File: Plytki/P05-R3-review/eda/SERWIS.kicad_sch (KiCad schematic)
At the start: 22 parts

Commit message: P05 R3 (S1) etap 2: typy części — SMD 1206, posiadane THT z rejestru, SW1 JS202011AQN
Rezystory precyzyjne 1206 0,1 %: okno DAQ_OK (R3-R8) 10 ppm/K, dzielniki
kanałów 25 ppm/K. Z rejestru: 47k i 4,7k MF0207 na stojąco, MKT 10n/100n,
MKS2 1u, C0G 1n, logika i 1N4148. Wyjątki: R1 1 W leżący, C1, C12/C13 1210.
SW1: suwak kątowy C&K JS202011AQN (biegun B lustrzany względem 7201).
ERC 0, 464/464 pinów.

Co-Authored-By: Claude Opus 5.5 <noreply@anthropic.com>
Claude-Session: https://claude.ai/code/session_01PNjhiJP63vXoN5NGrWe8up
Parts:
- R36, R37, R38, R44, R45, R46, R47, R48, R49, R50, R51, R52, R55: footprint Resistor_SMD:R_0805_2012Metric -> Resistor_SMD:R_1206_3216Metric_Pad1.30x1.75mm_HandSolder; MPN 0805 1% 0.125W 1K -> RC1206FR-071KL
- R39, R40, R41, R42, R53, R54: footprint Resistor_SMD:R_0805_2012Metric -> Resistor_SMD:R_1206_3216Metric_Pad1.30x1.75mm_HandSolder; MPN 0805 1% 0.125W 10K -> RC1206FR-0710KL
- R43: footprint Resistor_SMD:R_0805_2012Metric -> Resistor_THT:R_Axial_DIN0207_L6.3mm_D2.5mm_P5.08mm_Vertical; MPN 0805 1% 0.125W 4.7K -> MF0207FTE-4K7 (Yageo MF0207 1% 0.6W, owned, standing)

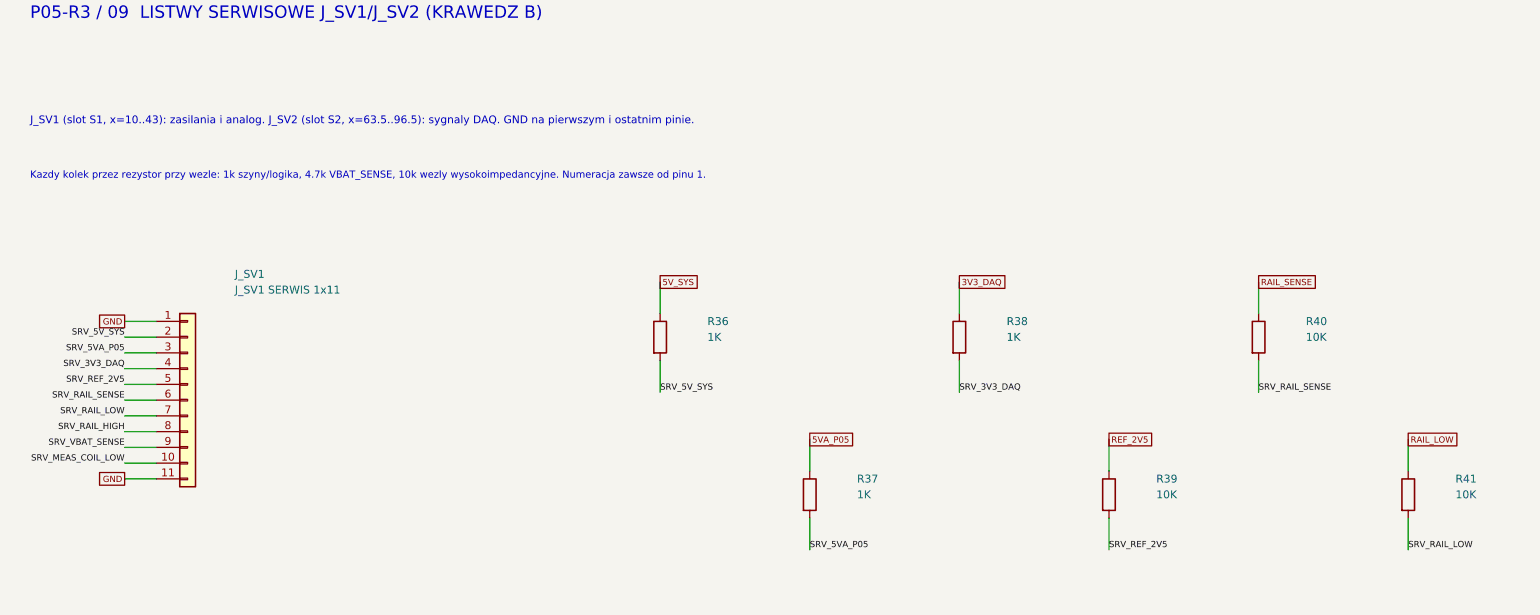
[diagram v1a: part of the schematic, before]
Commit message: P05 R3: poprawki po recenzji lokalnej PR #7 (SW1 czeka na decyzję)
- J_SV1 13 kołków: szyny 5V_SYS/5VA_P05/3V3_DAQ obok siebie i GND, VBAT_SENSE
  między GND (zasada z P03 R6); wewnętrzne GND 3 i 7; R36–R44 bez zmian
- bilans posiadanych części z P02 R4: MKT 10n/100n i WIMA 1µ zostają po 1 szt.,
  więc C2, C23, C16–C18, C25, C26 jako nowe 1206; BOM z kolumną zrodlo
- verify_s1: szyny tylko obok GND / szyn, GND na końcach (wewnątrz dozwolone),
  kolumna rezystorów w SERWIS.csv, nowe mutacje — 26/26, mutacje 33/33
- verify_electrical: budżet dzielników kanałów (0,1 %, 25 ppm/K) w raporcie
- README: punkt otwarty pojemności 5V_SYS (~986 µF wobec 600 µF) i SW1
  (E-Switch pionowy M2 ok. 28 mm wobec 16,5 mm; karta w reference/)
- ODBIOR: kołki J_SV1, pomiar REF_2V5 na C24 albo miernikiem >= 1 GOhm;
  U5B dla DAQ_OK; nieaktualne teksty R2 w PROJEKT, INTEGRACJA, DLA-RECENZENTA

Co-Authored-By: Claude Opus 5.5 <noreply@anthropic.com>
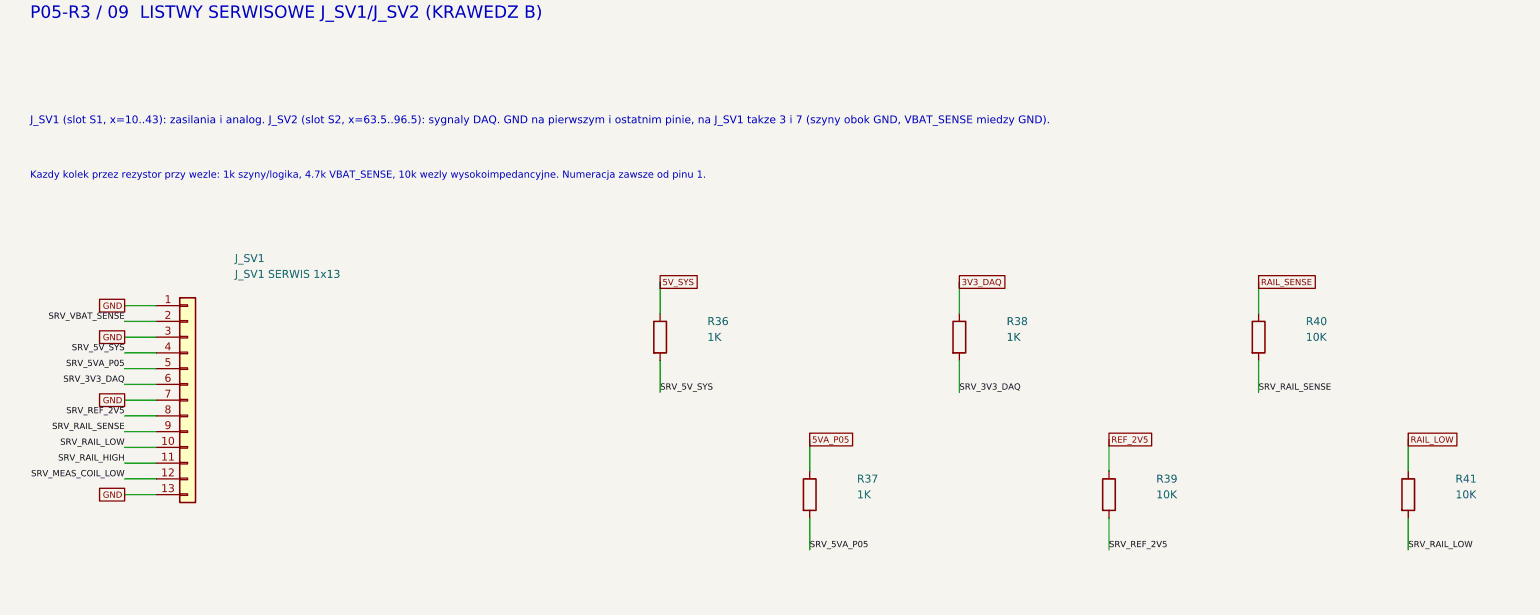
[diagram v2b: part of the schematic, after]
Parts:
- J_SV1: value J_SV1 SERWIS 1x11 -> J_SV1 SERWIS 1x13; footprint Connector_PinHeader_2.54mm:PinHeader_1x11_P2.54mm_Horizontal -> Connector_PinHeader_2.54mm:PinHeader_1x13_P2.54mm_Horizontal; symbol P05:Conn_01x11 -> P05:Conn_01x13; MPN Pin header 1x11, 2.54 mm, right angle, Au -> Pin header 1x13, 2.54 mm, right angle, Au
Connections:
- net GND: now also J_SV1.13 (Pin_13), J_SV1.3 (Pin_3), J_SV1.7 (Pin_7); no longer J_SV1.11 (Pin_11)
- net SRV_3V3_DAQ: now also J_SV1.6 (Pin_6); no longer J_SV1.4 (Pin_4)
- net SRV_5VA_P05: now also J_SV1.5 (Pin_5); no longer J_SV1.3 (Pin_3)
- net SRV_5V_SYS: now also J_SV1.4 (Pin_4); no longer J_SV1.2 (Pin_2)
- net SRV_MEAS_COIL_LOW: now also J_SV1.12 (Pin_12); no longer J_SV1.10 (Pin_10)
- net SRV_RAIL_HIGH: now also J_SV1.11 (Pin_11); no longer J_SV1.8 (Pin_8)
- net SRV_RAIL_LOW: now also J_SV1.10 (Pin_10); no longer J_SV1.7 (Pin_7)
- net SRV_RAIL_SENSE: now also J_SV1.9 (Pin_9); no longer J_SV1.6 (Pin_6)
- net SRV_REF_2V5: now also J_SV1.8 (Pin_8); no longer J_SV1.5 (Pin_5)
- net SRV_VBAT_SENSE: now also J_SV1.2 (Pin_2); no longer J_SV1.9 (Pin_9)
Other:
- note added: "J_SV1 (slot S1, x=10..43): zasilania i analog. J_SV2 (slot S2, x=63.5..96.5): sygnaly DAQ. GND na pierwszym i ostatnim pinie, na J_SV1 takze 3 i 7 (szyny obok GND, VBAT_SENSE miedzy GND)."
- note removed: "J_SV1 (slot S1, x=10..43): zasilania i analog. J_SV2 (slot S2, x=63.5..96.5): sygnaly DAQ. GND na pierwszym i ostatnim pinie."
